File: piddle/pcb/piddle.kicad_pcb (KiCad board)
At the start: 2 copper layers, 133.5 x 118 mm, 64 parts, among them J1 Conn_01x03_Socket, J10 Conn_01x03_Socket, J11 Conn_01x02_Socket, J12 Conn_01x02_Socket, J2 Conn_01x03_Socket, J3 Conn_01x03_Socket, J4 Conn_01x03_Socket, J5 Conn_01x03_Socket, J6 Conn_01x03_Socket, J7 Conn_01x03_Socket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

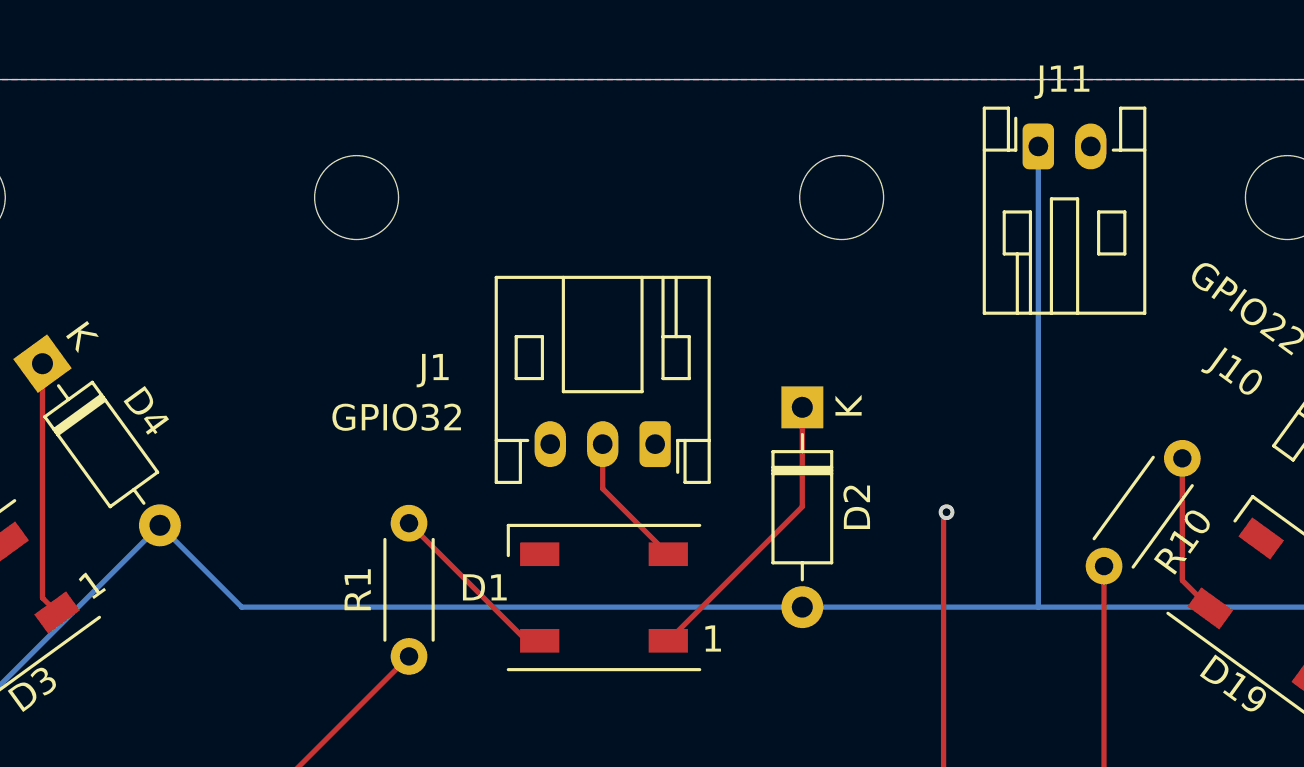
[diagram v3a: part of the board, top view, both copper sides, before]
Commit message: Add jumper for powering board from LED strip
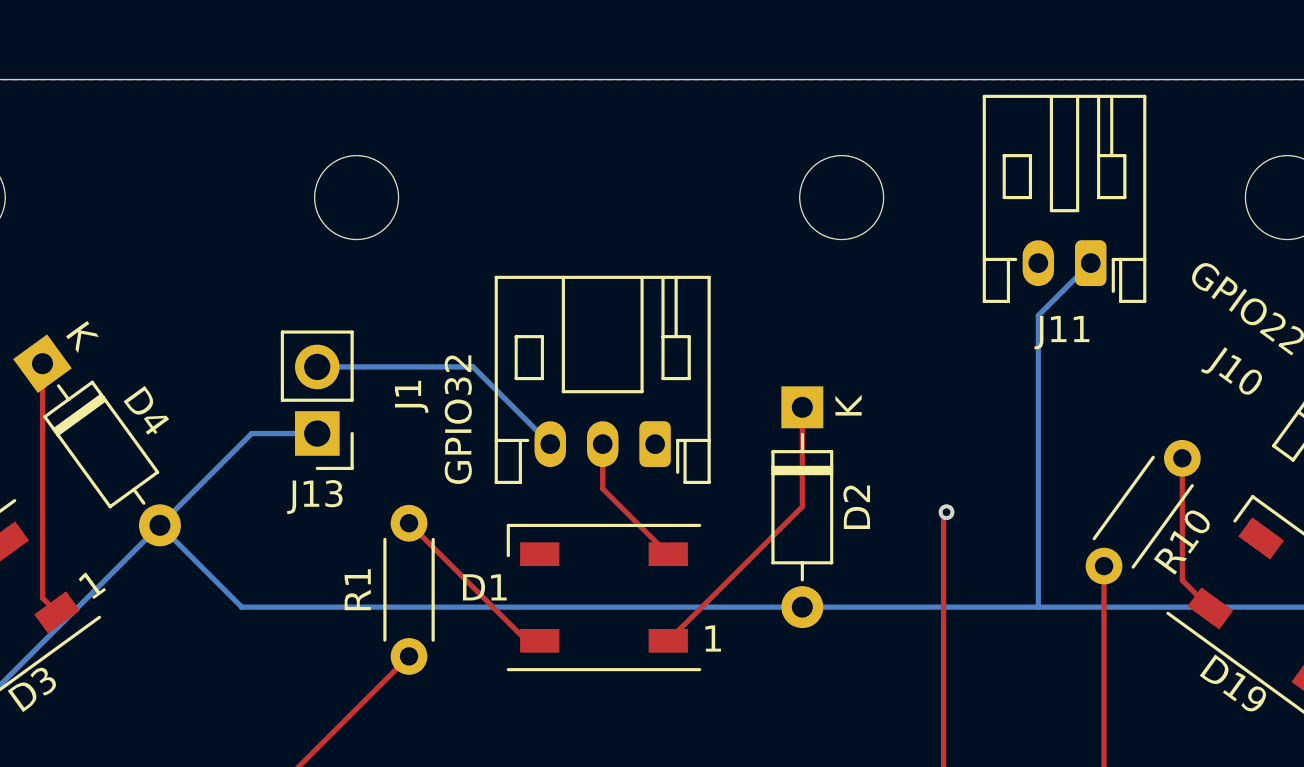
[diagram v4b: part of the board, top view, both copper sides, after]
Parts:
- added J13: Conn_01x02_Pin, Connector_PinHeader_2.54mm:PinHeader_1x02_P2.54mm_Vertical, F.Cu at (94.1, 67.6)
- moved J11 4.88 mm to (123.6, 61.1), turned to 180 degrees
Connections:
- J1 pad 3: unconnected-(J1-Pin_3-Pad3) -> Net-(J1-Pin_3)
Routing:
- net Net-(J1-Pin_3): track 0.00 -> 10.1 mm
- net +5V: track 242.1 -> 245.9 mm
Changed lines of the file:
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@@
   (net 35 "Net-(D1-VDD)")
   (net 36 "Net-(D1-DOUT)")
-  (net 37 "unconnected-(J1-Pin_3-Pad3)")
+  (net 37 "Net-(J1-Pin_3)")
   (net 38 "/GPIO32")
   (net 39 "Net-(D3-VDD)")
@@
     (property "ki_keywords" "connector")
     (attr through_hole)
-    (fp_text reference "J1" (at 8.38672 2.903657 180) (layer "F.SilkS")
+    (fp_text reference "J1" (at 9.38672 1.903657 270) (layer "F.SilkS")
         (effects (font (size 1 1) (thickness 0.15)))
     )
@@
       (net 36 "Net-(D1-DOUT)") (pinfunction "Pin_2") (pintype "passive"))
     (pad "3" thru_hole oval (at 4 0 180) (size 1.2 1.75) (drill 0.75) (layers "*.Cu" "*.Mask")
-      (net 37 "unconnected-(J1-Pin_3-Pad3)") (pinfunction "Pin_3") (pintype "passive"))
+      (net 37 "Net-(J1-Pin_3)") (pinfunction "Pin_3") (pintype "passive"))
     (model "${KICAD6_3DMODEL_DIR}/Connector_JST.3dshapes/JST_PH_S3B-PH-K_1x03_P2.00mm_Horizontal.wrl"
       (offset (xyz 0 0 0))
@@
     (pad "" np_thru_hole circle (at 0 0) (size 3.2 3.2) (drill 3.2) (layers "F&B.Cu" "*.Mask"))
   )
+  (footprint "Connector_PinHeader_2.54mm:PinHeader_1x02_P2.54mm_Vertical" (layer "F.Cu")
+    (at 94.11328 67.596343 180)
+    (descr "Through hole straight pin header, 1x02, 2.54mm pitch, single row")
+    (tags "Through hole pin header THT 1x02 2.54mm single row")
+    (property "Sheetfile" "piddle.kicad_sch")
+    (property "Sheetname" "")
+    (property "ki_description" "Generic connector, single row, 01x02, script generated")
+    (property "ki_keywords" "connector")
+    (attr through_hole)
+    (fp_text reference "J13" (at 0 -2.33) (layer "F.SilkS")
+        (effects (font (size 1 1) (thickness 0.15)))
+    )
+    (fp_text value "Conn_01x02_Pin" (at 0 4.87) (layer "F.Fab")
+        (effects (font (size 1 1) (thickness 0.15)))
+    )
+    (fp_text user "${REFERENCE}" (at 0 1.27 90) (layer "F.Fab")
+        (effects (font (size 1 1) (thickness 0.15)))
+    )
+    (fp_line (start -1.33 -1.33) (end 0 -1.33)
+      (stroke (width 0.12) (type solid)) (layer "F.SilkS"))
+    (fp_line (start -1.33 0) (end -1.33 -1.33)
+      (stroke (width 0.12) (type solid)) (layer "F.SilkS"))
+    (fp_line (start -1.33 1.27) (end -1.33 3.87)
+      (stroke (width 0.12) (type solid)) (layer "F.SilkS"))
+    (fp_line (start -1.33 1.27) (end 1.33 1.27)
+      (stroke (width 0.12) (type solid)) (layer "F.SilkS"))
+    (fp_line (start -1.33 3.87) (end 1.33 3.87)
+      (stroke (width 0.12) (type solid)) (layer "F.SilkS"))
+    (fp_line (start 1.33 1.27) (end 1.33 3.87)
+      (stroke (width 0.12) (type solid)) (layer "F.SilkS"))
+    (fp_line (start -1.8 -1.8) (end -1.8 4.35)
+      (stroke (width 0.05) (type solid)) (layer "F.CrtYd"))
+    (fp_line (start -1.8 4.35) (end 1.8 4.35)
+      (stroke (width 0.05) (type solid)) (layer "F.CrtYd"))
+    (fp_line (start 1.8 -1.8) (end -1.8 -1.8)
+      (stroke (width 0.05) (type solid)) (layer "F.CrtYd"))
+    (fp_line (start 1.8 4.35) (end 1.8 -1.8)
+      (stroke (width 0.05) (type solid)) (layer "F.CrtYd"))
+    (fp_line (start -1.27 -0.635) (end -0.635 -1.27)
+      (stroke (width 0.1) (type solid)) (layer "F.Fab"))
+    (fp_line (start -1.27 3.81) (end -1.27 -0.635)
+      (stroke (width 0.1) (type solid)) (layer "F.Fab"))
+    (fp_line (start -0.635 -1.27) (end 1.27 -1.27)
+      (stroke (width 0.1) (type solid)) (layer "F.Fab"))
+    (fp_line (start 1.27 -1.27) (end 1.27 3.81)
+      (stroke (width 0.1) (type solid)) (layer "F.Fab"))
+    (fp_line (start 1.27 3.81) (end -1.27 3.81)
+      (stroke (width 0.1) (type solid)) (layer "F.Fab"))
+    (pad "1" thru_hole rect (at 0 0 180) (size 1.7 1.7) (drill 1) (layers "*.Cu" "*.Mask")
+      (net 12 "+5V") (pinfunction "Pin_1") (pintype "passive"))
+    (pad "2" thru_hole oval (at 0 2.54 180) (size 1.7 1.7) (drill 1) (layers "*.Cu" "*.Mask")
+      (net 37 "Net-(J1-Pin_3)") (pinfunction "Pin_2") (pintype "passive"))
+    (model "${KICAD6_3DMODEL_DIR}/Connector_PinHeader_2.54mm.3dshapes/PinHeader_1x02_P2.54mm_Vertical.wrl"
+      (offset (xyz 0 0 0))
+      (scale (xyz 1 1 1))
+      (rotate (xyz 0 0 0))
+    )
+  )
   (footprint "Resistor_THT:R_Axial_DIN0204_L3.6mm_D1.6mm_P5.08mm_Horizontal" (layer "F.Cu")
     (at 76.61328 80.596343 126)
@@
   )
   (footprint "Connector_JST:JST_PH_S2B-PH-K_1x02_P2.00mm_Horizontal" (layer "F.Cu")
-    (at 121.61328 56.646343)
+    (at 123.61328 61.096343 180)
     (descr "JST PH series connector, S2B-PH-K (http://www.jst-mfg.com/product/pdf/eng/ePH.pdf), generated with kicad-footprint-generator")
     (tags "connector JST PH top entry")
@@
     (fp_line (start 3.95 6.25) (end 3.95 -1.35)
       (stroke (width 0.1) (type solid)) (layer "F.Fab"))
-    (pad "1" thru_hole roundrect (at 0 0) (size 1.2 1.75) (drill 0.75) (layers "*.Cu" "*.Mask") (roundrect_rratio 0.208333)
+    (pad "1" thru_hole roundrect (at 0 0 180) (size 1.2 1.75) (drill 0.75) (layers "*.Cu" "*.Mask") (roundrect_rratio 0.208333)
       (net 12 "+5V") (pinfunction "Pin_1") (pintype "passive"))
-    (pad "2" thru_hole oval (at 2 0) (size 1.2 1.75) (drill 0.75) (layers "*.Cu" "*.Mask")
+    (pad "2" thru_hole oval (at 2 0 180) (size 1.2 1.75) (drill 0.75) (layers "*.Cu" "*.Mask")
       (net 1 "GND") (pinfunction "Pin_2") (pintype "passive"))
     (model "${KICAD6_3DMODEL_DIR}/Connector_JST.3dshapes/JST_PH_S2B-PH-K_1x02_P2.00mm_Horizontal.wrl"
@@
     (effects (font (size 1 1) (thickness 0.1)) (justify left bottom))
   )
-  (gr_text "GPIO32" (at 94.61328 67.596343) (layer "F.SilkS")
+  (gr_text "GPIO32" (at 100.11328 69.596343 90) (layer "F.SilkS")
     (effects (font (size 1 1) (thickness 0.1)) (justify left bottom))
   )
@@
   (segment (start 137.134356 79.261052) (end 137.134356 98.219179) (width 0.2) (layer "B.Cu") (net 12))
   (segment (start 121.61328 74.216343) (end 132.089647 74.216343) (width 0.2) (layer "B.Cu") (net 12))
+  (segment (start 94.11328 67.596343) (end 91.61328 67.596343) (width 0.2) (layer "B.Cu") (net 12))
   (segment (start 92.6 138.00272) (end 91.825218 138.00272) (width 0.2) (layer "B.Cu") (net 12))
   (segment (start 78.11328 81.096343) (end 88.11328 71.096343) (width 0.2) (layer "B.Cu") (net 12))
@@
   (segment (start 132.089647 74.216343) (end 137.134356 79.261052) (width 0.2) (layer "B.Cu") (net 12))
   (segment (start 138.514803 122.241634) (end 144.366229 122.241634) (width 0.2) (layer "B.Cu") (net 12))
+  (segment (start 121.61328 63.096343) (end 121.61328 74.216343) (width 0.2) (layer "B.Cu") (net 12))
   (segment (start 78.11328 87.596343) (end 78.11328 81.096343) (width 0.2) (layer "B.Cu") (net 12))
   (segment (start 77.747107 121.73017) (end 64.11328 108.096343) (width 0.2) (layer "B.Cu") (net 12))
   (segment (start 140.866229 118.741634) (end 144.366229 122.241634) (width 0.2) (layer "B.Cu") (net 12))
+  (segment (start 123.61328 61.096343) (end 121.61328 63.096343) (width 0.2) (layer "B.Cu") (net 12))
   (segment (start 97.61328 143.016) (end 92.6 138.00272) (width 0.2) (layer "B.Cu") (net 12))
   (segment (start 77.747107 123.924609) (end 77.747107 121.73017) (width 0.2) (layer "B.Cu") (net 12))
   (segment (start 91.23328 74.216343) (end 112.61328 74.216343) (width 0.2) (layer "B.Cu") (net 12))
   (segment (start 64.11328 108.096343) (end 64.11328 101.596343) (width 0.2) (layer "B.Cu") (net 12))
-  (segment (start 121.61328 56.646343) (end 121.61328 74.216343) (width 0.2) (layer "B.Cu") (net 12))
+  (segment (start 91.61328 67.596343) (end 88.11328 71.096343) (width 0.2) (layer "B.Cu") (net 12))
   (segment (start 91.825218 138.00272) (end 77.747107 123.924609) (width 0.2) (layer "B.Cu") (net 12))
   (segment (start 137.134356 98.219179) (end 140.866229 101.951052) (width 0.2) (layer "B.Cu") (net 12))
@@
   (segment (start 105 69.7) (end 107.5 72.2) (width 0.2) (layer "F.Cu") (net 36))
   (segment (start 105 68) (end 105 69.7) (width 0.2) (layer "F.Cu") (net 36))
+  (segment (start 94.11328 65.056343) (end 100.056343 65.056343) (width 0.2) (layer "B.Cu") (net 37))
+  (segment (start 100.056343 65.056343) (end 103 68) (width 0.2) (layer "B.Cu") (net 37))
   (segment (start 97.61328 76.096343) (end 87.61328 86.096343) (width 0.2) (layer "F.Cu") (net 38))
   (segment (start 87.61328 102.536) (end 92.6 107.52272) (width 0.2) (layer "F.Cu") (net 38))

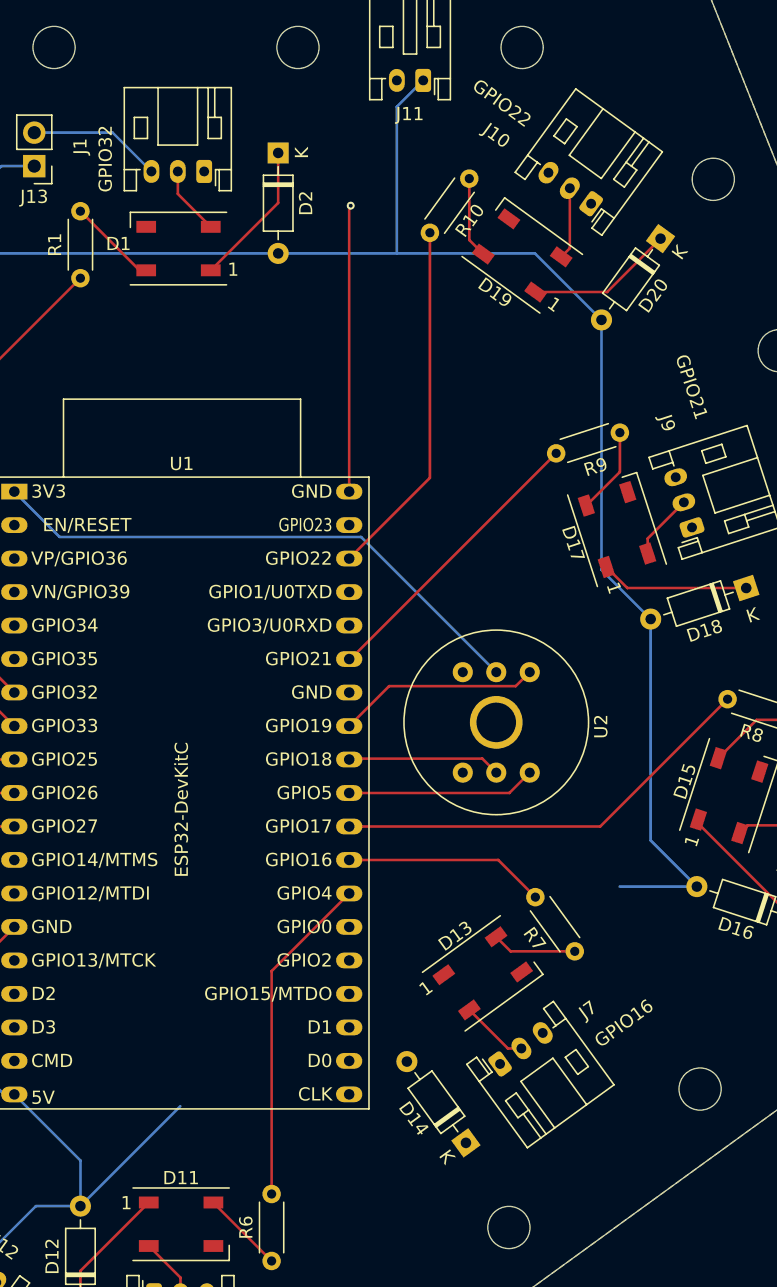
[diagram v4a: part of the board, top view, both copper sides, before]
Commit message: More connections
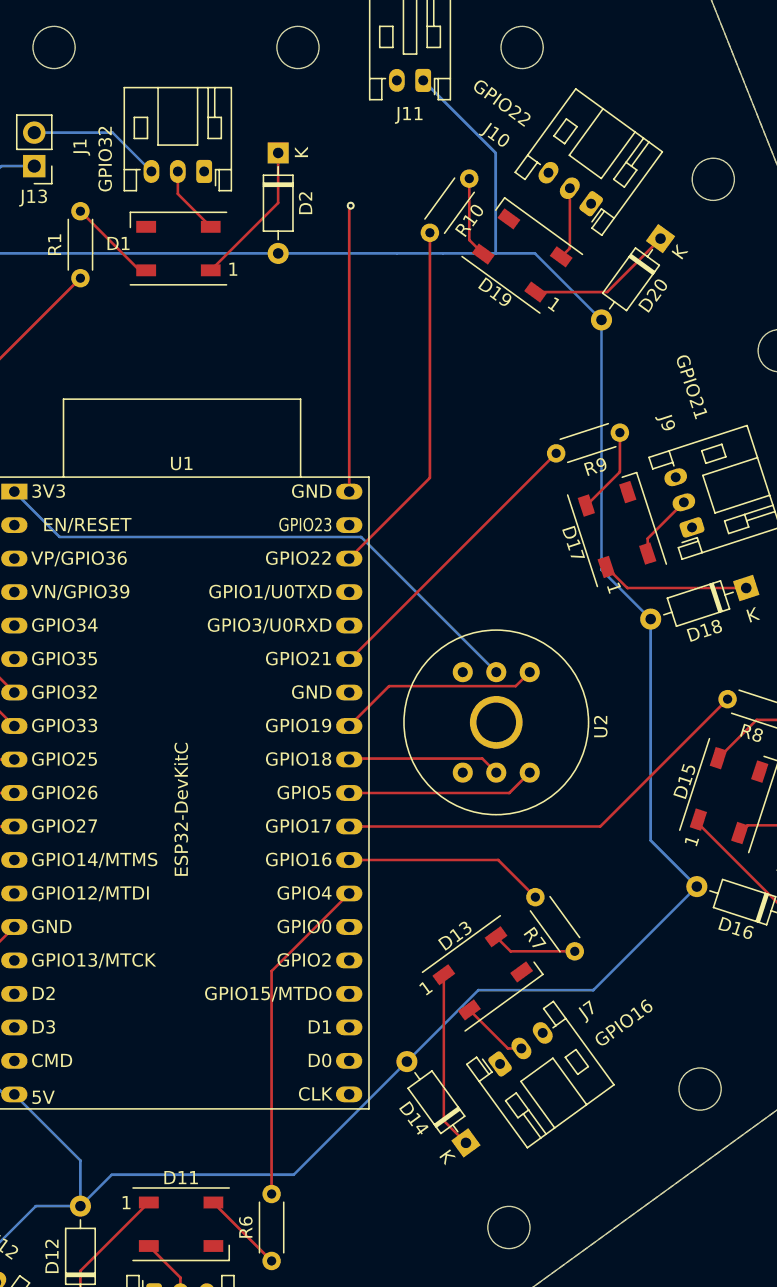
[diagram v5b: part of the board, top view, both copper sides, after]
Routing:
- net +5V: track 245.9 -> 287.6 mm
- net Net-(D13-VDD): track 0.00 -> 13.4 mm
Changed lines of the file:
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@@
   (segment (start 85.979026 117.68272) (end 82.058377 121.603369) (width 0.2) (layer "F.Cu") (net 9))
   (segment (start 92.6 117.68272) (end 85.979026 117.68272) (width 0.2) (layer "F.Cu") (net 9))
+  (segment (start 125.120306 74.209317) (end 125.11328 74.216343) (width 0.2) (layer "B.Cu") (net 12))
+  (segment (start 113.791464 144.096343) (end 122.373818 135.513989) (width 0.2) (layer "B.Cu") (net 12))
   (segment (start 64.11328 101.596343) (end 78.11328 87.596343) (width 0.2) (layer "B.Cu") (net 12))
+  (segment (start 136.51152 130.096343) (end 127.791464 130.096343) (width 0.2) (layer "B.Cu") (net 12))
   (segment (start 112.61328 74.216343) (end 121.61328 74.216343) (width 0.2) (layer "B.Cu") (net 12))
+  (segment (start 97.61328 146.476343) (end 99.99328 144.096343) (width 0.2) (layer "B.Cu") (net 12))
+  (segment (start 129.11328 66.596343) (end 129.11328 74.216343) (width 0.2) (layer "B.Cu") (net 12))
   (segment (start 137.134356 79.261052) (end 137.134356 98.219179) (width 0.2) (layer "B.Cu") (net 12))
-  (segment (start 121.61328 74.216343) (end 132.089647 74.216343) (width 0.2) (layer "B.Cu") (net 12))
   (segment (start 94.11328 67.596343) (end 91.61328 67.596343) (width 0.2) (layer "B.Cu") (net 12))
+  (segment (start 129.11328 74.216343) (end 132.089647 74.216343) (width 0.2) (layer "B.Cu") (net 12))
+  (segment (start 121.61328 74.216343) (end 125.11328 74.216343) (width 0.2) (layer "B.Cu") (net 12))
   (segment (start 92.6 138.00272) (end 91.825218 138.00272) (width 0.2) (layer "B.Cu") (net 12))
   (segment (start 78.11328 81.096343) (end 88.11328 71.096343) (width 0.2) (layer "B.Cu") (net 12))
-  (segment (start 105.189623 138.9) (end 97.61328 146.476343) (width 0.2) (layer "B.Cu") (net 12))
   (segment (start 132.089647 74.216343) (end 137.134356 79.261052) (width 0.2) (layer "B.Cu") (net 12))
-  (segment (start 138.514803 122.241634) (end 144.366229 122.241634) (width 0.2) (layer "B.Cu") (net 12))
-  (segment (start 121.61328 63.096343) (end 121.61328 74.216343) (width 0.2) (layer "B.Cu") (net 12))
   (segment (start 78.11328 87.596343) (end 78.11328 81.096343) (width 0.2) (layer "B.Cu") (net 12))
   (segment (start 77.747107 121.73017) (end 64.11328 108.096343) (width 0.2) (layer "B.Cu") (net 12))
   (segment (start 140.866229 118.741634) (end 144.366229 122.241634) (width 0.2) (layer "B.Cu") (net 12))
-  (segment (start 123.61328 61.096343) (end 121.61328 63.096343) (width 0.2) (layer "B.Cu") (net 12))
   (segment (start 97.61328 143.016) (end 92.6 138.00272) (width 0.2) (layer "B.Cu") (net 12))
   (segment (start 77.747107 123.924609) (end 77.747107 121.73017) (width 0.2) (layer "B.Cu") (net 12))
   (segment (start 91.23328 74.216343) (end 112.61328 74.216343) (width 0.2) (layer "B.Cu") (net 12))
   (segment (start 64.11328 108.096343) (end 64.11328 101.596343) (width 0.2) (layer "B.Cu") (net 12))
+  (segment (start 99.99328 144.096343) (end 113.791464 144.096343) (width 0.2) (layer "B.Cu") (net 12))
+  (segment (start 144.366229 122.241634) (end 136.51152 130.096343) (width 0.2) (layer "B.Cu") (net 12))
+  (segment (start 127.791464 130.096343) (end 122.373818 135.513989) (width 0.2) (layer "B.Cu") (net 12))
   (segment (start 91.61328 67.596343) (end 88.11328 71.096343) (width 0.2) (layer "B.Cu") (net 12))
+  (segment (start 123.61328 61.096343) (end 129.11328 66.596343) (width 0.2) (layer "B.Cu") (net 12))
   (segment (start 91.825218 138.00272) (end 77.747107 123.924609) (width 0.2) (layer "B.Cu") (net 12))
   (segment (start 137.134356 98.219179) (end 140.866229 101.951052) (width 0.2) (layer "B.Cu") (net 12))
@@
   (segment (start 89.61328 151.096343) (end 94.23328 146.476343) (width 0.2) (layer "B.Cu") (net 12))
   (segment (start 88.11328 71.096343) (end 91.23328 74.216343) (width 0.2) (layer "B.Cu") (net 12))
+  (segment (start 125.11328 74.216343) (end 129.11328 74.216343) (width 0.2) (layer "B.Cu") (net 12))
   (segment (start 97.61328 146.476343) (end 97.61328 143.016) (width 0.2) (layer "B.Cu") (net 12))
   (segment (start 112.11328 145.556343) (end 112.11328 128.64944) (width 0.2) (layer "F.Cu") (net 23))
@@
   (segment (start 105.2 153.2) (end 105.2 151.9) (width 0.2) (layer "F.Cu") (net 49))
   (segment (start 105.2 151.9) (end 102.8 149.5) (width 0.2) (layer "F.Cu") (net 49))
+  (segment (start 125.173589 139.999545) (end 125.173589 128.926587) (width 0.2) (layer "F.Cu") (net 50))
+  (segment (start 126.852742 141.678698) (end 125.173589 139.999545) (width 0.2) (layer "F.Cu") (net 50))
   (segment (start 130.034845 134.517908) (end 127.11328 131.596343) (width 0.2) (layer "F.Cu") (net 51))
   (segment (start 131.059926 134.517908) (end 130.034845 134.517908) (width 0.2) (layer "F.Cu") (net 51))
